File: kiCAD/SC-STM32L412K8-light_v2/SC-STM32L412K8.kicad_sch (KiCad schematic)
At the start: 70 parts, among them J1 usb, J10 gnd, J11 Vibro, J12 +2.8v, J13 +vibro, J14 gndBT, J15 -BAT, J16 +2.8v, J2 +29.6 SiPM, J3 TxD(20)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

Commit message: удалено:       kiCAD/SC-STM32L412K8-light_v2/SC-STM32L412K8-backups/SC-STM32L412K8-2023-09-11_154928.zip 	изменено:      kiCAD/SC-STM32L412K8-light_v2/SC-STM32L412K8.kicad_pcb 	изменено:      kiCAD/SC-STM32L412K8-light_v2/SC-STM32L412K8.kicad_prl 	изменено:      kiCAD/SC-STM32L412K8-light_v2/SC-STM32L412K8.kicad_sch 	изменено:      kiCAD/SC-STM32L412K8-light_v2/fp-info-cache 	изменено:      kiCAD/SC-STM32L412K8-light_v2/gerber/Border.gbr 	изменено:      kiCAD/SC-STM32L412K8-light_v2/gerber/Bottom.gbr 	изменено:      kiCAD/SC-STM32L412K8-light_v2/gerber/MaskBottom.gbr 	изменено:      kiCAD/SC-STM32L412K8-light_v2/gerber/MaskTop.gbr 	изменено:      kiCAD/SC-STM32L412K8-light_v2/gerber/NCData.drl 	изменено:      kiCAD/SC-STM32L412K8-light_v2/gerber/SC-STM32L412K8-job.gbrjob 	изменено:      kiCAD/SC-STM32L412K8-light_v2/gerber/SC-STM32L412K8.zip 	изменено:      kiCAD/SC-STM32L412K8-light_v2/gerber/Top.gbr
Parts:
- J13: footprint My-library:SMD-CONN -> lib:conn_mini
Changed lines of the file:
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@@
     )
     (property "Value" "+vibro" (id 1) (at 161.29 67.31 90))
-    (property "Footprint" "My-library:SMD-CONN" (id 2) (at 161.29 68.58 0)
+    (property "Footprint" "lib:conn_mini" (id 2) (at 161.29 68.58 0)
       (effects (font (size 1.27 1.27)) hide)
     )
@@
     )
     (path "/00000000-0000-0000-0000-00006052b033"
-      (reference "J13") (unit 1) (value "+vibro") (footprint "My-library:SMD-CONN")
+      (reference "J13") (unit 1) (value "+vibro") (footprint "lib:conn_mini")
     )
     (path "/00000000-0000-0000-0000-000061532825"

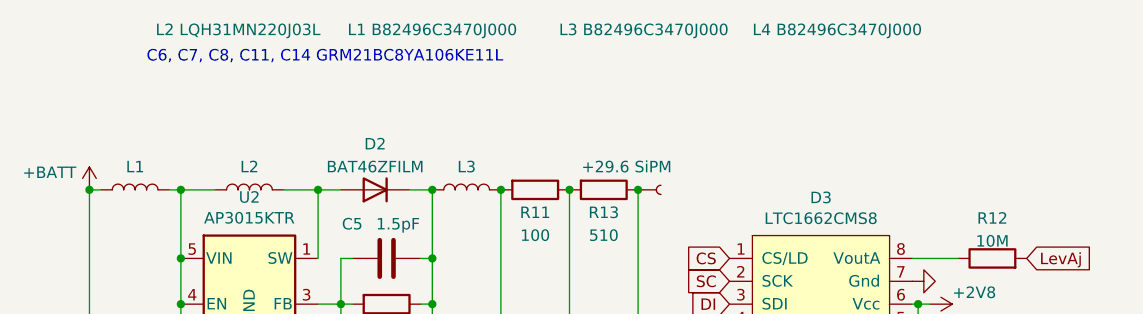
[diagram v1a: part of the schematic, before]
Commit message: изменено:      kiCAD/SC-STM32L412K8-light_v2/SC-STM32L412K8.kicad_prl 	изменено:      kiCAD/SC-STM32L412K8-light_v2/SC-STM32L412K8.kicad_sch 	изменено:      kiCAD/SC-STM32L412K8-light_v2/fp-info-cache 	изменено:      stm32Cube/STM32L412K8code/.settings/language.settings.xml
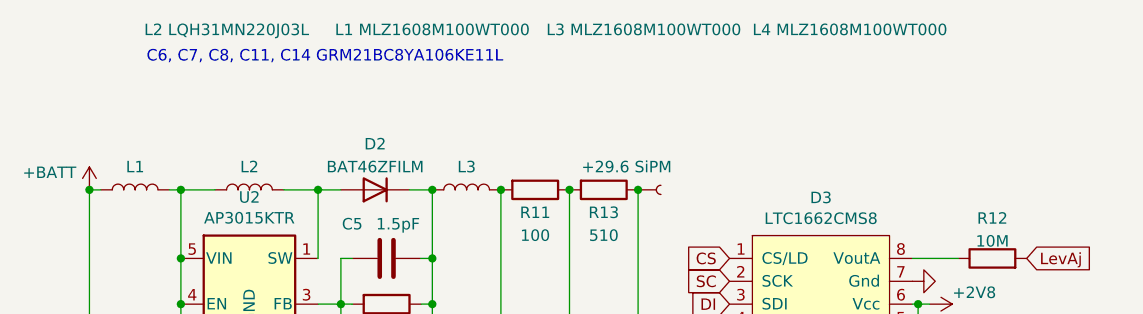
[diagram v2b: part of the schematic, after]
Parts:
- L1: value L1 B82496C3470J000 -> L1 MLZ1608M100WT000
- L3: value L3 B82496C3470J000 -> L3 MLZ1608M100WT000
- L4: value L4 B82496C3470J000 -> L4 MLZ1608M100WT000
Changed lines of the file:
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@@
     (in_bom yes) (on_board yes)
     (property "Reference" "L2" (id 0) (at 116.84 30.48 90))
-    (property "Value" "L2 LQH31MN220J03L" (id 1) (at 115.57 15.24 90))
+    (property "Value" "L2 LQH31MN220J03L" (id 1) (at 114.3 15.24 90))
     (property "Footprint" "Inductor_SMD:L_1210_3225Metric" (id 2) (at 116.84 33.02 0)
       (effects (font (size 1.27 1.27)) hide)
@@
       (effects (font (size 1.27 1.27)) (justify left))
     )
-    (property "Value" "L4 B82496C3470J000" (id 1) (at 172.72 15.24 0)
+    (property "Value" "L4 MLZ1608M100WT000" (id 1) (at 172.72 15.24 0)
       (effects (font (size 1.27 1.27)) (justify left))
     )
@@
     (in_bom yes) (on_board yes)
     (property "Reference" "L1" (id 0) (at 104.14 30.48 90))
-    (property "Value" "L1 B82496C3470J000" (id 1) (at 137.16 15.24 90))
+    (property "Value" "L1 MLZ1608M100WT000" (id 1) (at 137.16 15.24 90))
     (property "Footprint" "Inductor_SMD:L_0603_1608Metric" (id 2) (at 104.14 33.02 0)
       (effects (font (size 1.27 1.27)) hide)
@@
     (in_bom yes) (on_board yes)
     (property "Reference" "L3" (id 0) (at 140.97 30.48 90))
-    (property "Value" "L3 B82496C3470J000" (id 1) (at 160.655 15.24 90))
+    (property "Value" "L3 MLZ1608M100WT000" (id 1) (at 160.655 15.24 90))
     (property "Footprint" "Inductor_SMD:L_0603_1608Metric" (id 2) (at 140.97 33.02 0)
       (effects (font (size 1.27 1.27)) hide)
@@
     )
     (path "/00000000-0000-0000-0000-000060436bf5"
-      (reference "L1") (unit 1) (value "L1 B82496C3470J000") (footprint "Inductor_SMD:L_0603_1608Metric")
+      (reference "L1") (unit 1) (value "L1 MLZ1608M100WT000") (footprint "Inductor_SMD:L_0603_1608Metric")
     )
     (path "/00000000-0000-0000-0000-0000603653a2"
@@
     )
     (path "/00000000-0000-0000-0000-000060437de2"
-      (reference "L3") (unit 1) (value "L3 B82496C3470J000") (footprint "Inductor_SMD:L_0603_1608Metric")
+      (reference "L3") (unit 1) (value "L3 MLZ1608M100WT000") (footprint "Inductor_SMD:L_0603_1608Metric")
     )
     (path "/00000000-0000-0000-0000-00006037b2e7"
-      (reference "L4") (unit 1) (value "L4 B82496C3470J000") (footprint "Inductor_SMD:L_0603_1608Metric")
+      (reference "L4") (unit 1) (value "L4 MLZ1608M100WT000") (footprint "Inductor_SMD:L_0603_1608Metric")
     )
     (path "/00000000-0000-0000-0000-0000609a9fba"
